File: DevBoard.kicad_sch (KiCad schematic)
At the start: 135 parts, among them J1 Audio_In, J10 Jumper, J11 RJ45, J12 Jumper, J13 Jumper, J14 Jumper, J15 Jumper, J16 Jumper, J17 Jumper, J18 DAC_I2S, J19 DAC_OUT, J2 Audio_In, J20 DAC_Amplified, J21 DAC_Amplified, J22 Voltmeter_Power, J23 Voltmeter_Positive, J24 Voltmeter_Ground, J25 Conn_01x05_Pin, J26 Pot1, J27 Pot2, J28 Pot3, J29 Pot4, J3 Audio_Amplified, J30 CV_Scaled_Out1, J31 Audio12V_In, J32 Audio_Scaled_Out, J33 CV_In2, J34 Power, J35 Power, J36 Power, J37 Power, J38 Power, J39 Power_Test, J4 Audio_Amplified, J40 Power, J41 Power_Test, J42 Power, J43 Power, J44 Pot1, J45 Pot2, J46 Pot3, J47 Pot4, J48 CV_In1, J49 CV_Scaled_Out2, J5 CV_In, J50 Audio12V_In, J51 Audio_Scaled_Out, J6 CV_In, J7 CV_Amplified, J8 CV_Amplified, J9 Jumper, SW2 SW_DPDT_x2, U1 MCP6004, U2 TL074, U3 LM1117-3.3, U4 LM1117-5.0, U5 LM4040DBZ-5, U6 PCM5100APW, U8 TL072

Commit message: Further layout
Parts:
- removed C10: 1uF, Capacitor_SMD:C_0805_2012Metric, symbol Device:C_Small
- added D3, D4: 5V_LED, LED_SMD:LED_0603_1608Metric, symbol Device:LED_Small
- added R36, R37: 2k2, Resistor_SMD:R_0805_2012Metric, symbol Device:R_Small
- D1: value LED_Small -> 12V_LED
- D2: value LED_Small -> -12V_LED
- J6: value CV_In -> CV_Out
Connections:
- net +12V: no longer C9.2, U1.4 (V+)
- net +3.3VA: now also C9.2, U1.4 (V+)
- net +5V: now also R36.1, R37.1
- net -12V: no longer U1.11 (V-)
- net Audio_In1: now also J1.2 (Pin_2); no longer J2.1 (Pin_1)
- net Audio_In2: now also J3.2 (Pin_2); no longer J4.1 (Pin_1)
- net Audio_Out1: now also J2.1 (Pin_1); no longer J1.2 (Pin_2)
- net Audio_Out2: now also J4.1 (Pin_1); no longer J3.2 (Pin_2)
- net Audio_Scaled1: now also U1.1; no longer U1.7
- net Audio_Scaled2: now also U1.14; no longer U1.1
- net CV1_In: now also J5.2 (Pin_2); no longer J6.1 (Pin_1)
- net CV1_Out: now also J6.1 (Pin_1); no longer J5.2 (Pin_2)
- net CV2_In: now also J7.2 (Pin_2); no longer J8.1 (Pin_1)
- net CV2_Out: now also J8.1 (Pin_1); no longer J7.2 (Pin_2)
- net CV_Scaled_Out1: now also U1.7; no longer U1.8
- net CV_Scaled_Out2: now also U1.8; no longer U1.14
- net DAC_OUT_AMP_L: now also J20.2 (Pin_2); no longer J21.1 (Pin_1)
- net DAC_OUT_AMP_R: now also J21.1 (Pin_1); no longer J20.2 (Pin_2)
- net GND: now also U1.10 (+), U1.11 (V-), U1.12 (+), U1.3 (+), U1.5 (+), D3.1 (K), D4.1 (K); no longer U1.10 (+), U1.12 (+), U1.3 (+), U1.5 (+)
- net at C4.2, R12.2, R7.1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: now also U1.9 (-); no longer U1.13 (-)
- net at C2.2, R10.2, R3.1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: now also U1.13 (-); no longer U1.2 (-)
- net at C3.2, R11.2, R5.1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: now also U1.6 (-); no longer U1.9 (-)
- net at C1.2, R1.1, R2.1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: now also U1.2 (-); no longer U1.6 (-)
- new net: D4.2 (A), R37.2
- new net: D3.2 (A), R36.2
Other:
- moved on the sheet: D1, R27

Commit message: PCB Updates
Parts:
- D4: value 5V_LED -> 3V3_LED
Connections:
- net +3V3: now also R37.1
- net +5V: no longer R37.1
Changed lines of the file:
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@@
       (effects (font (size 1.27 1.27)))
     )
-    (property "Value" "5V_LED" (at 149.86 72.39 0)
+    (property "Value" "3V3_LED" (at 149.86 72.39 0)
       (effects (font (size 1.27 1.27)))
     )
@@
     )
   )
+  (symbol (lib_id "power:+3.3V") (at 139.7 67.31 90) (unit 1)
+    (in_bom yes) (on_board yes) (dnp no) (fields_autoplaced)
+    (property "Reference" "#PWR019" (at 143.51 67.31 0)
+      (effects (font (size 1.27 1.27)) hide)
+    )
+    (property "Value" "+3.3V" (at 135.89 67.945 90)
+      (effects (font (size 1.27 1.27)) (justify left))
+    )
+    (property "Footprint" "" (at 139.7 67.31 0)
+      (effects (font (size 1.27 1.27)) hide)
+    )
+    (property "Datasheet" "" (at 139.7 67.31 0)
+      (effects (font (size 1.27 1.27)) hide)
+    )
+    (pin "1")
+    (instances
+      (project "DevBoard"
+        (path "/cf927a28-c7bc-4509-acea-70dea4ea1f8a"
+          (reference "#PWR019") (unit 1)
+        )
+      )
+    )
+  )
   (symbol (lib_id "Device:R_Small") (at 143.51 93.98 90) (mirror x) (unit 1)
     (in_bom yes) (on_board yes) (dnp no)
@@
         )
       )
-    )
-  )
-  (symbol (lib_id "power:+5V") (at 139.7 67.31 90) (unit 1)
-    (in_bom yes) (on_board yes) (dnp no) (fields_autoplaced)
-    (property "Reference" "#PWR097" (at 143.51 67.31 0)
-      (effects (font (size 1.27 1.27)) hide)
-    )
-    (property "Value" "+5V" (at 135.89 67.945 90)
-      (effects (font (size 1.27 1.27)) (justify left))
-    )
-    (property "Footprint" "" (at 139.7 67.31 0)
-      (effects (font (size 1.27 1.27)) hide)
-    )
-    (property "Datasheet" "" (at 139.7 67.31 0)
-      (effects (font (size 1.27 1.27)) hide)
-    )
-    (pin "1")
-    (instances
-      (project "DevBoard"
-        (path "/cf927a28-c7bc-4509-acea-70dea4ea1f8a"
-          (reference "#PWR097") (unit 1)
-        )
-      )

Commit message: First draft routing completed
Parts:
- removed J24: Voltmeter_Ground, TestPoint:TestPoint_Pad_4.0x4.0mm, symbol Connector:Conn_01x01_Pin
- removed J26: Pot1, Connector_PinHeader_2.54mm:PinHeader_1x01_P2.54mm_Vertical, symbol Connector:Conn_01x01_Pin
- removed J27: Pot2, Connector_PinHeader_2.54mm:PinHeader_1x01_P2.54mm_Vertical, symbol Connector:Conn_01x01_Pin
- removed J28: Pot3, Connector_PinHeader_2.54mm:PinHeader_1x01_P2.54mm_Vertical, symbol Connector:Conn_01x01_Pin
- removed J29: Pot4, Connector_PinHeader_2.54mm:PinHeader_1x01_P2.54mm_Vertical, symbol Connector:Conn_01x01_Pin
- removed J34, J35, J36, J37, J38, J42, J43: Power, Connector_PinHeader_2.54mm:PinHeader_1x02_P2.54mm_Vertical, symbol Connector:Conn_01x02_Pin
- added J26: DAC_I2S, Connector_PinSocket_2.54mm:PinSocket_1x03_P2.54mm_Vertical, symbol Connector:Conn_01x03_Pin
- added J35: Conn_01x06_Socket, Connector_PinSocket_2.54mm:PinSocket_1x06_P2.54mm_Vertical, symbol Connector:Conn_01x06_Socket
- added J52: Conn_01x04_Pin, Connector_PinSocket_2.54mm:PinSocket_1x04_P2.54mm_Vertical, symbol Connector:Conn_01x04_Pin
- added U7: ~, Custom_Footprints:MiniVoltmeter, symbol Mountjoy:MiniVoltmeter
- C30: footprint Capacitor_SMD:CP_Elec_4x5.8 -> Capacitor_SMD:CP_Elec_5x5.4
- J1, J20, J3, J30, J40, J49, J51, J6, J8: footprint Connector_PinHeader_2.54mm:PinHeader_1x02_P2.54mm_Vertical -> Connector_PinSocket_2.54mm:PinSocket_1x02_P2.54mm_Vertical
- J22: value Voltmeter_Power -> Voltmeter; footprint TestPoint:TestPoint_Pad_4.0x4.0mm -> Connector_PinSocket_2.54mm:PinSocket_1x01_P2.54mm_Vertical
- J23: value Voltmeter_Positive -> Power_Test
- J25: footprint Connector_PinHeader_2.54mm:PinHeader_1x05_P2.54mm_Vertical -> Connector_PinSocket_2.54mm:PinSocket_1x05_P2.54mm_Vertical
- J31: value Audio12V_In -> AudioToMCU; footprint Connector_PinHeader_2.54mm:PinHeader_1x02_P2.54mm_Vertical -> Connector_PinSocket_2.54mm:PinSocket_1x02_P2.54mm_Vertical
- J50: value Audio12V_In -> AudioToMCU
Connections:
- net +VDC is gone; now on net GND: J23.1 (Pin_1)
- net +12V: now also J35.5 (Pin_5), U7.2 (PowerIn); no longer J22.1 (Pin_1)
- net +3.3VA: now also J35.2 (Pin_2)
- net +3V3: now also J35.1 (Pin_1)
- net +5V: now also J35.3 (Pin_3)
- net -12V: now also J35.6 (Pin_6)
- net -5V: now also J35.4 (Pin_4)
- net Audio12V_In1: now also J50.1 (Pin_1); no longer J31.2 (Pin_2)
- net Audio12V_In2: now also J32.1 (Pin_1); no longer J51.2 (Pin_2)
- net Audio_In1: now also J2.1 (Pin_1); no longer J1.2 (Pin_2)
- net Audio_In2: now also J4.1 (Pin_1); no longer J3.2 (Pin_2)
- net Audio_Out1: now also J1.2 (Pin_2); no longer J2.1 (Pin_1)
- net Audio_Out2: now also J3.2 (Pin_2); no longer J4.1 (Pin_1)
- net CV1_In: now also J6.1 (Pin_1); no longer J5.2 (Pin_2)
- net CV1_Out: now also J5.2 (Pin_2); no longer J6.1 (Pin_1)
- net CV2_In: now also J8.1 (Pin_1); no longer J7.2 (Pin_2)
- net CV2_Out: now also J7.2 (Pin_2); no longer J8.1 (Pin_1)
- net CV_In1: now also J30.1 (Pin_1); no longer J48.2 (Pin_2)
- net CV_In2: now also J49.1 (Pin_1); no longer J33.2 (Pin_2)
- net CV_Scaled_Out1: now also J48.2 (Pin_2); no longer J30.1 (Pin_1)
- net CV_Scaled_Out2: now also J33.2 (Pin_2); no longer J49.1 (Pin_1)
- net DAC_BCLK: now also J26.3 (Pin_3)
- net DAC_DATA: now also J26.2 (Pin_2)
- net DAC_LRCLK: now also J26.1 (Pin_1)
- net DAC_OUT_AMP_L: now also J21.1 (Pin_1); no longer J20.2 (Pin_2)
- net DAC_OUT_AMP_R: now also J20.2 (Pin_2); no longer J21.1 (Pin_1)
- net GND: now also U7.3 (Ground)
- net Pot2: now reaches J45.1 (Pin_1), RV2.2
- net Pot2: now also J52.2 (Pin_2)
- net Pot3: now reaches J46.1 (Pin_1), RV3.2
- net Pot3: now also J52.3 (Pin_3)
- net Pot4: now reaches J47.1 (Pin_1), RV4.2
- net Pot4: now also J52.4 (Pin_4)
- net Pot1: now reaches J44.1 (Pin_1), RV1.2
- net Pot1: now also J52.1 (Pin_1)
- net Audio_Scaled1 renamed Audio_Scaled_Out1
- net Audio_Scaled_Out1: now also J31.2 (Pin_2); no longer J50.1 (Pin_1)
- net Audio_Scaled2 renamed Audio_Scaled_Out2
- net Audio_Scaled_Out2: now also J51.2 (Pin_2); no longer J32.1 (Pin_1)
- new net Voltmeter_In: J22.1 (Pin_1), U7.1 (VoltmeterIn)
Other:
- moved on the sheet: J30, J44, J45, J46, J47, J49, J6, J8

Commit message: Cleaned up schematic
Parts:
- removed C1, C2, C24, C25, C3, C4: 1nF, Capacitor_SMD:C_0805_2012Metric, symbol Device:C_Small
- removed C16, C17, C19, C23: 100nF, Capacitor_SMD:C_0805_2012Metric, symbol Device:C_Small
- removed C18, C22, C5, C6: 10uF, Capacitor_SMD:C_0805_2012Metric, symbol Device:C_Small
- removed C20, C21: 2.2uF, Capacitor_SMD:C_0805_2012Metric, symbol Device:C_Small
- removed C26, C27: 100pF, Capacitor_SMD:C_0805_2012Metric, symbol Device:C_Small
- removed C28, C29, C7, C8, C9: 1uF, Capacitor_SMD:C_0805_2012Metric, symbol Device:C_Small
- removed J1: Audio_In, Connector_PinSocket_2.54mm:PinSocket_1x02_P2.54mm_Vertical, symbol Connector:Conn_01x02_Pin
- removed J18: DAC_I2S, Connector_PinHeader_2.54mm:PinHeader_1x03_P2.54mm_Vertical, symbol Connector:Conn_01x03_Pin
- removed J19: DAC_OUT, Connector_PinHeader_2.54mm:PinHeader_1x02_P2.54mm_Vertical, symbol Connector:Conn_01x02_Pin
- removed J2: Audio_In, Connector_PinHeader_2.54mm:PinHeader_1x02_P2.54mm_Vertical, symbol Connector:Conn_01x02_Pin
- removed J20: DAC_Amplified, Connector_PinSocket_2.54mm:PinSocket_1x02_P2.54mm_Vertical, symbol Connector:Conn_01x02_Pin
- removed J21: DAC_Amplified, Connector_PinHeader_2.54mm:PinHeader_1x02_P2.54mm_Vertical, symbol Connector:Conn_01x02_Pin
- removed J26: DAC_I2S, Connector_PinSocket_2.54mm:PinSocket_1x03_P2.54mm_Vertical, symbol Connector:Conn_01x03_Pin
- removed J3: Audio_Amplified, Connector_PinSocket_2.54mm:PinSocket_1x02_P2.54mm_Vertical, symbol Connector:Conn_01x02_Pin
- removed J30: CV_Scaled_Out1, Connector_PinSocket_2.54mm:PinSocket_1x02_P2.54mm_Vertical, symbol Connector:Conn_01x02_Pin
- removed J31: AudioToMCU, Connector_PinSocket_2.54mm:PinSocket_1x02_P2.54mm_Vertical, symbol Connector:Conn_01x02_Pin
- removed J32: Audio_Scaled_Out, Connector_PinHeader_2.54mm:PinHeader_1x02_P2.54mm_Vertical, symbol Connector:Conn_01x02_Pin
- removed J33: CV_In2, Connector_PinHeader_2.54mm:PinHeader_1x02_P2.54mm_Vertical, symbol Connector:Conn_01x02_Pin
- removed J4: Audio_Amplified, Connector_PinHeader_2.54mm:PinHeader_1x02_P2.54mm_Vertical, symbol Connector:Conn_01x02_Pin
- removed J48: CV_In1, Connector_PinHeader_2.54mm:PinHeader_1x02_P2.54mm_Vertical, symbol Connector:Conn_01x02_Pin
- removed J49: CV_Scaled_Out2, Connector_PinSocket_2.54mm:PinSocket_1x02_P2.54mm_Vertical, symbol Connector:Conn_01x02_Pin
- removed J5: CV_In, Connector_PinHeader_2.54mm:PinHeader_1x02_P2.54mm_Vertical, symbol Connector:Conn_01x02_Pin
- removed J50: AudioToMCU, Connector_PinHeader_2.54mm:PinHeader_1x02_P2.54mm_Vertical, symbol Connector:Conn_01x02_Pin
- removed J51: Audio_Scaled_Out, Connector_PinSocket_2.54mm:PinSocket_1x02_P2.54mm_Vertical, symbol Connector:Conn_01x02_Pin
- removed J6: CV_Out, Connector_PinSocket_2.54mm:PinSocket_1x02_P2.54mm_Vertical, symbol Connector:Conn_01x02_Pin
- removed J7: CV_Amplified, Connector_PinHeader_2.54mm:PinHeader_1x02_P2.54mm_Vertical, symbol Connector:Conn_01x02_Pin
- removed J8: CV_Amplified, Connector_PinSocket_2.54mm:PinSocket_1x02_P2.54mm_Vertical, symbol Connector:Conn_01x02_Pin
- removed R1, R3: 20k, Resistor_SMD:R_0805_2012Metric, symbol Device:R
- removed R10, R9: 6k8, Resistor_SMD:R_0805_2012Metric, symbol Device:R
- removed R11, R12, R2, R34, R35, R4: 47k, Resistor_SMD:R_0805_2012Metric, symbol Device:R
- removed R13, R14: 3k3, Resistor_SMD:R_0805_2012Metric, symbol Device:R_Small
- removed R15, R16: 47k, Resistor_SMD:R_0805_2012Metric, symbol Device:R_Small
- removed R17, R18: 2k7, Resistor_SMD:R_0805_2012Metric, symbol Device:R_Small
- removed R19, R20: 4k7, Resistor_SMD:R_0805_2012Metric, symbol Device:R_Small
- removed R21, R22: 10k, Resistor_SMD:R_0805_2012Metric, symbol Device:R_Small
- removed R23, R24, R25, R26: 1k, Resistor_SMD:R_0805_2012Metric, symbol Device:R_Small
- removed R30, R31: 2k2, Resistor_SMD:R_0805_2012Metric, symbol Device:R
- removed R32, R33: 10k, Resistor_SMD:R_0805_2012Metric, symbol Device:R
- removed R5, R7: 68k, Resistor_SMD:R_0805_2012Metric, symbol Device:R
- removed R6, R8: 100k, Resistor_SMD:R_0805_2012Metric, symbol Device:R
- removed U1: MCP6004, Package_SO:SOIC-14_3.9x8.7mm_P1.27mm, symbol Amplifier_Operational:MCP6004
- removed U2: TL074, Package_SO:SOIC-14_3.9x8.7mm_P1.27mm, symbol Amplifier_Operational:TL074
- removed U6: PCM5100APW, Custom_Footprints:SSOP-20_4.4x6.5mm_Pitch0.65mm_Round_Pads, symbol PCM5100APW:PCM5100APW
- removed U8: TL072, Package_SO:SOIC-8_3.9x4.9mm_P1.27mm, symbol Amplifier_Operational:TL072
- J23, J39, J41: value Power_Test -> Ground
- J25: value Conn_01x05_Pin -> Interconnects
- J35: value Conn_01x06_Socket -> Power
- J40: value Power -> Ground
- J52: value Conn_01x04_Pin -> Pot_Out
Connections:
- net +3V3 renamed +3.3V
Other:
- added sheet DAC (DAC.kicad_sch)
- added sheet EurorackToMCU (EurorackToMCU.kicad_sch)
- added sheet MCUToEurorack (MCUToEurorack.kicad_sch)
- note added: "Eurorack In"
- note added: "Indicators"
- note added: "Potentiometers"
- note added: "Power"
- note added: "Signal Conditioning and DAC"
- note added: "Voltage Regulators"
- note removed: "= 1.7 - A_{IN} * 0.144 = 0 For A_{IN} = 11.8v; 3.3 for -11.1v"
- note removed: "= 3.46 - A_{IN} * 0.47 = 0 For A_{IN} = 7.36v; 3.3 for 0.34v"
- note removed: "Audio to MCU Scaling"
- note removed: "CV to MCU Scaling"
- note removed: "FLT: connect to ground for higher latency but less ringing"
- note removed: "Full Scale: 7V"
- note removed: "Gain 2.42: 0v - 3.3v > 0v - 8v"
- note removed: "HP Filter cutoff = 0.33Hz Gain = 4.7: 0-3.3v > +/-7.8v"
- note removed: "MCU to Audio Amplifiers"
- note removed: "MCU to CV Amplifiers"
- note removed: "V_{out} = 5 * (47k / 68k) - A_{IN} * (47k / 100k)"
- note removed: "V_{out} = 5 * (6.8k / 20k) - A_{IN} * (6.8k / 47k)"
- company: (none) -> Mountjoy Modular
- title: (none) -> Eurorack Dev Board
- moved on the sheet: C11, C12, C13, C14, C30, C31, D1, D2, D3, D4, H1, H2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

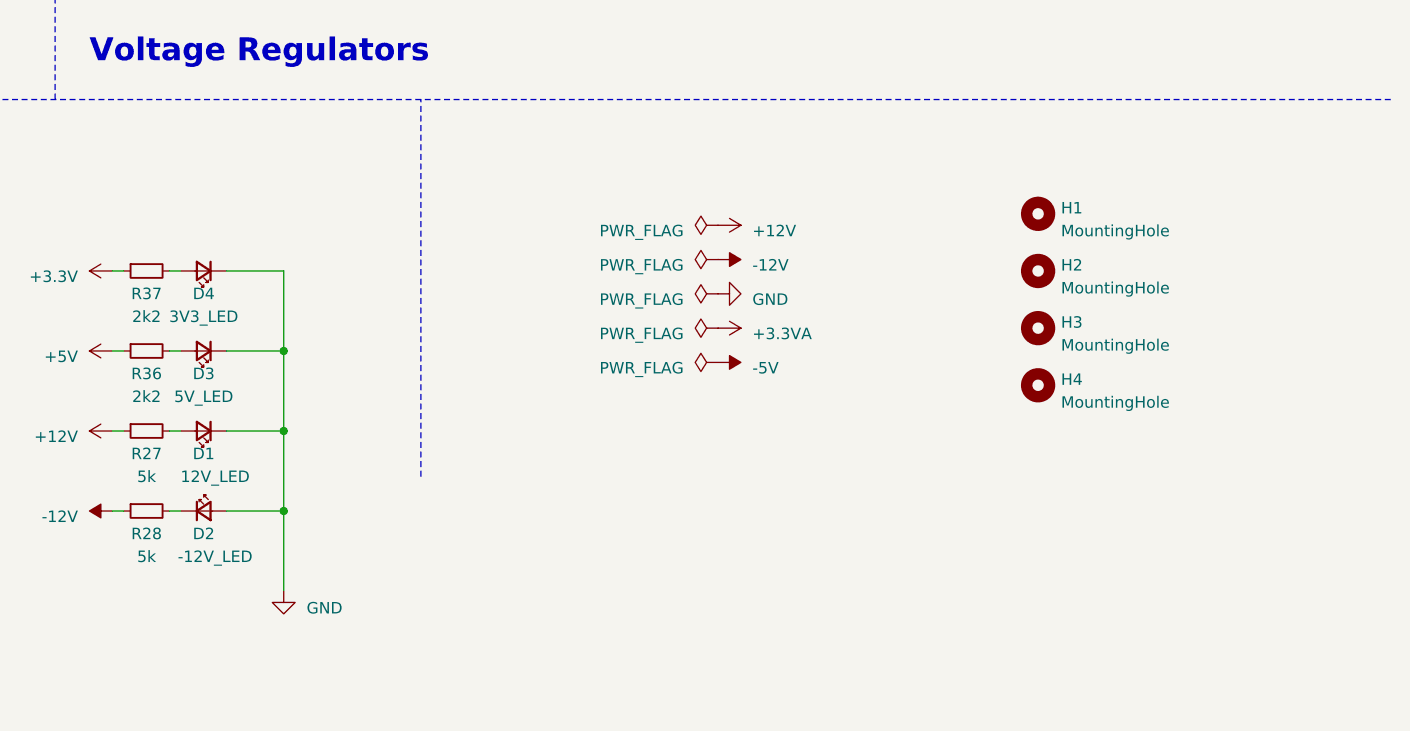
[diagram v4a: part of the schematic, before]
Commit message: Layout tweaks
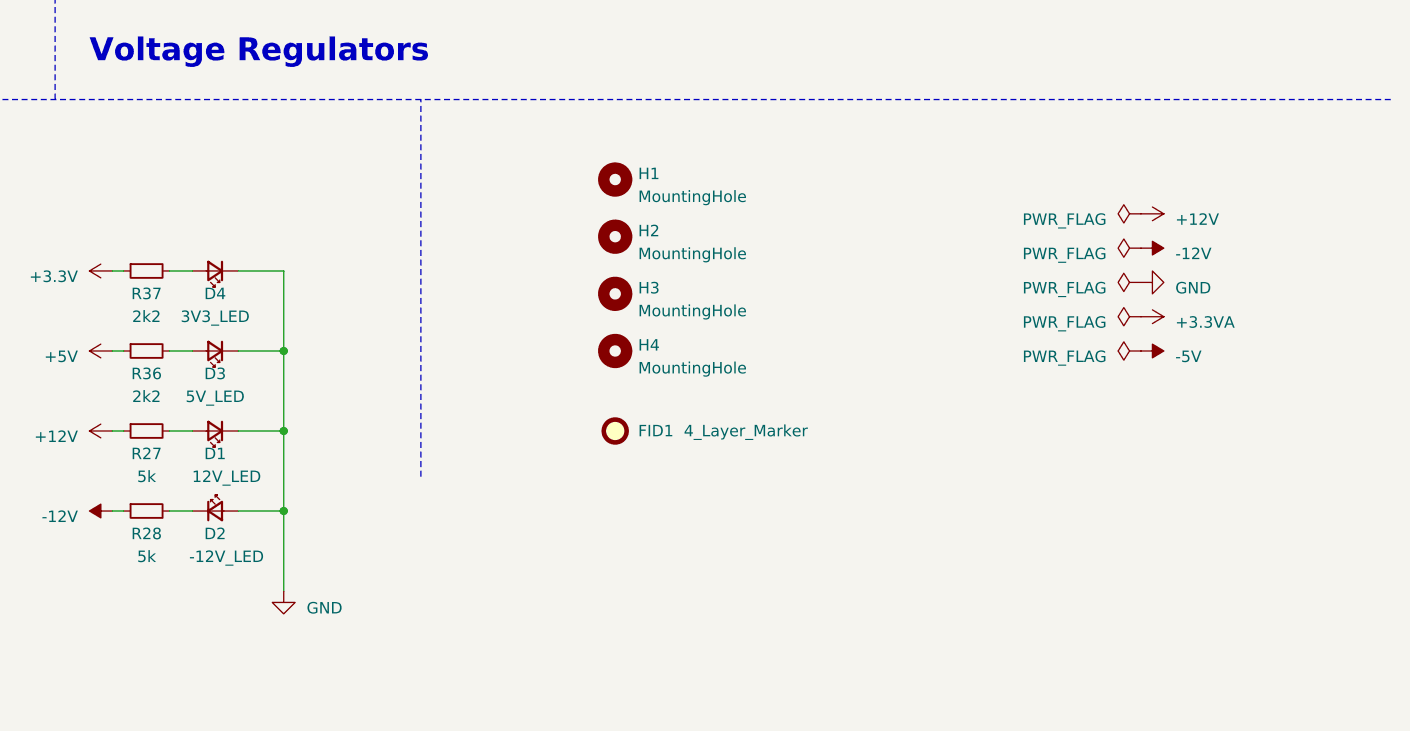
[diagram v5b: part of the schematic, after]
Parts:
- added FID1: 4_Layer_Marker, Custom_Footprints:4_Layer_Markers, symbol Mechanical:Fiducial
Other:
- moved on the sheet: D1, D2, D3, D4, H1, H2, H3, H4

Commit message: Preparing for production
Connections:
- net Interconnect4_GATE renamed Interconnect4
- net Interconnect5_CV renamed Interconnect5
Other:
- moved on the sheet: C13
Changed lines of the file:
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@@
+    (stroke (width 0) (type default))
+  )
+  (wire (pts (xy 180.34 96.52) (xy 180.34 95.25))
     (stroke (width 0) (type default))
   )
@@
     (stroke (width 0) (type default))
   )
-  (wire (pts (xy 180.34 104.14) (xy 180.34 100.33))
+  (wire (pts (xy 180.34 104.14) (xy 180.34 101.6))
     (stroke (width 0) (type default))
   )
@@
     (effects (font (size 1.27 1.27)) (justify left bottom))
   )
-  (label "Interconnect4_GATE" (at 96.52 36.83 0) (fields_autoplaced)
+  (label "Interconnect4" (at 96.52 36.83 0) (fields_autoplaced)
     (effects (font (size 1.27 1.27)) (justify left bottom))
   )
-  (label "Interconnect4_GATE" (at 50.8 43.18 0) (fields_autoplaced)
+  (label "Interconnect4" (at 50.8 43.18 0) (fields_autoplaced)
     (effects (font (size 1.27 1.27)) (justify left bottom))
   )
@@
     (effects (font (size 1.27 1.27)) (justify left bottom))
   )
-  (label "Interconnect5_CV" (at 50.8 40.64 0) (fields_autoplaced)
+  (label "Interconnect5" (at 50.8 40.64 0) (fields_autoplaced)
     (effects (font (size 1.27 1.27)) (justify left bottom))
   )
@@
     (effects (font (size 1.27 1.27)) (justify left bottom))
   )
-  (label "Interconnect5_CV" (at 96.52 34.29 0) (fields_autoplaced)
+  (label "Interconnect5" (at 96.52 34.29 0) (fields_autoplaced)
     (effects (font (size 1.27 1.27)) (justify left bottom))
   )
@@
     )
   )
-  (symbol (lib_id "Device:C_Small") (at 180.34 97.79 0) (unit 1)
-    (in_bom yes) (on_board yes) (dnp no) (fields_autoplaced)
-    (property "Reference" "C13" (at 182.88 97.1613 0)
-      (effects (font (size 1.27 1.27)) (justify left))
-    )
-    (property "Value" "10uF" (at 182.88 99.7013 0)
-      (effects (font (size 1.27 1.27)) (justify left))
-    )
-    (property "Footprint" "Capacitor_SMD:C_0805_2012Metric" (at 180.34 97.79 0)
-      (effects (font (size 1.27 1.27)) hide)
-    )
-    (property "Datasheet" "~" (at 180.34 97.79 0)
+  (symbol (lib_id "Device:C_Small") (at 180.34 99.06 0) (unit 1)
+    (in_bom yes) (on_board yes) (dnp no) (fields_autoplaced)
+    (property "Reference" "C13" (at 182.88 98.4313 0)
+      (effects (font (size 1.27 1.27)) (justify left))
+    )
+    (property "Value" "10uF" (at 182.88 100.9713 0)
+      (effects (font (size 1.27 1.27)) (justify left))
+    )
+    (property "Footprint" "Capacitor_SMD:C_0805_2012Metric" (at 180.34 99.06 0)
+      (effects (font (size 1.27 1.27)) hide)
+    )
+    (property "Datasheet" "~" (at 180.34 99.06 0)
       (effects (font (size 1.27 1.27)) hide)
     )
@@
       (effects (font (size 1.27 1.27)) hide)
     )
-    (property "Value" "+12V" (at 207.01 26.67 0)
+    (property "Value" "+12V" (at 207.01 27.94 0)
       (effects (font (size 1.27 1.27)) (justify left))
     )
@@
       (effects (font (size 1.27 1.27)) hide)
     )
-    (property "Value" "+12V" (at 161.29 26.67 0)
+    (property "Value" "+12V" (at 161.29 27.94 0)
       (effects (font (size 1.27 1.27)) (justify left))
     )
@@
       (effects (font (size 1.27 1.27)) hide)
     )
-    (property "Value" "+12V" (at 231.14 26.67 0)
+    (property "Value" "+12V" (at 231.14 27.94 0)
       (effects (font (size 1.27 1.27)) (justify left))
     )
@@
       (effects (font (size 1.27 1.27)) hide)
     )
-    (property "Value" "+12V" (at 184.15 26.67 0)
-      (effects (font (size 1.27 1.27)) (justify left))
-    )
+    (property "Value" "+12V" (at 184.15 27.94 0)
+      (effects (font (size 1.27 1.27)) (justify left))
+    )
